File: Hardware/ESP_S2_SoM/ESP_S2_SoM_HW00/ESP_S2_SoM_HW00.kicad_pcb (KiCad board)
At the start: 6 copper layers, 29.5 x 24.7 mm, 55 parts, among them J1 DF40C-60DP-0.4V(51), J2 Bare PCB USB C, SW401 SW_Push, SW402 SW_Push, U201 BQ24075RGTR, U301 MIC5528-3.3YMT-T5, U401 ESP32-S2FH4, Y601 Crystal_GND24_Small

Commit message: ESP32 data is done
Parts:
- moved C407 21.5 mm to (136.7, 91.0), turned to 45 degrees
- moved L401 20.9 mm to (135.6, 90.4), turned to -45 degrees
- moved C406 19.9 mm to (134.5, 90.3), turned to -90 degrees
- moved ANT401 14.9 mm to (129.5, 90.3), turned to 180 degrees
- moved C401 3.19 mm to (127.8, 92.8), turned to 180 degrees
- moved C402 3.02 mm to (127.8, 96.0), turned to 0 degrees
- moved Y601 2.85 mm to (127.8, 94.4), turned to 90 degrees
- moved R406 2.21 mm to (133.9, 95.4)
- moved R405 2.21 mm to (134.5, 94.8)
- moved R407 2.21 mm to (135.0, 94.3)
- moved R408 2.21 mm to (133.4, 95.9)
- moved C410 1.17 mm to (138.0, 93.1)
- moved C403 1.17 mm to (129.9, 95.7)
- moved C404 1.17 mm to (132.6, 92.4)
- moved C408 1.17 mm to (135.1, 91.9)
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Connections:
- J1 pad 42: IO39 -> IO41 (x2)
- J1 pad 44: IO40 -> IO39 (x2)
- J1 pad 46: IO41 -> IO40 (x2)
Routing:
- net IO0: track 0.00 -> 16.7 mm, vias 0 -> 2
- net /100_Connectors/D+: track 14.9 -> 19.9 mm
- net Net-(C401-Pad1): track 1.98 -> 4.11 mm
- net Net-(U401-XTAL_N): track 5.15 -> 7.28 mm
- net IO18: track 5.65 -> 7.55 mm, vias 0 -> 1
- net IO8: track 9.76 -> 11.3 mm
- net SPI6: track 8.13 -> 6.59 mm
- net IO33: track 15.2 -> 16.6 mm
- net /100_Connectors/D-: track 16.2 -> 17.4 mm
- net IO41: track 19.5 -> 18.3 mm
- net SPI5: track 5.61 -> 4.60 mm
- net IO38: track 15.1 -> 16.1 mm
- net SPI4: track 5.68 -> 4.77 mm
- net IO5: track 11.7 -> 12.5 mm
- net IO14: track 7.39 -> 8.20 mm
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
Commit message: working on power routing
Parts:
- moved R101 1.60 mm to (128.6, 108.0)
- moved R102 1.60 mm to (128.6, 108.0)
- moved C404 0.83 mm to (132.6, 91.6), turned to 90 degrees
- moved C402 0.40 mm to (127.8, 95.6)
- moved Y601 0.40 mm to (127.8, 94.0)
- moved C401 0.40 mm to (127.8, 92.4)
- moved R403 0.33 mm to (133.9, 91.6), turned to -90 degrees
- moved C414 0.30 mm to (133.2, 91.6), turned to 90 degrees
- moved ANT401 0.22 mm to (129.6, 90.1)
- moved C403 0.17 mm to (130.0, 95.8)
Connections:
- J1 pad 10: unconnected-(J1-Pad10) -> VBUS (x2)
- J1 pad 12: unconnected-(J1-Pad12) -> VBUS (x2)
- J1 pad 14: unconnected-(J1-Pad14) -> /VSYS (x2)
- J1 pad 16: unconnected-(J1-Pad16) -> /VSYS (x2)
- J1 pad 18: unconnected-(J1-Pad18) -> +3V3 (x2)
- J1 pad 20: unconnected-(J1-Pad20) -> +3V3 (x2)
- J1 pad 22: unconnected-(J1-Pad22) -> GND (x2)
- J1 pad 24: unconnected-(J1-Pad24) -> GND (x2)
- J1 pad 4: unconnected-(J1-Pad4) -> /VBAT (x2)
- J1 pad 48: /100_Connectors/TX0 -> /100_Connectors/RX0 (x2)
- J1 pad 50: /100_Connectors/RX0 -> /100_Connectors/TX0 (x2)
- J1 pad 6: unconnected-(J1-Pad6) -> /VBAT (x2)
- J1 pad 8: unconnected-(J1-Pad8) -> /VBAT (x2)
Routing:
- net GND: track 1.91 -> 34.4 mm, vias 32 -> 65
- net VBUS: track 5.60 -> 37.5 mm, vias 0 -> 4
- net /VBAT: track 1.81 -> 22.7 mm
- net /400_ESP32/EN: track 1.89 -> 17.9 mm, vias 0 -> 2
- net IO15: track 6.40 -> 21.4 mm, vias 0 -> 2
- net +3V3: track 11.6 -> 25.7 mm, vias 0 -> 11
- net /100_Connectors/CC2: track 0.00 -> 4.38 mm, vias 0 -> 2
- net /100_Connectors/CC1: track 0.00 -> 3.57 mm
- net SPI6: track 6.59 -> 8.76 mm
- net /100_Connectors/D+: track 19.9 -> 18.2 mm, vias 2 -> 1
- net IO42: track 16.5 -> 15.3 mm
- net IO33: track 16.6 -> 15.8 mm
- net /100_Connectors/D-: track 17.4 -> 17.1 mm, vias 2 -> 1

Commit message: Routing is done
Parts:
- added C101: 100n, Capacitor_SMD:C_0201_0603Metric, B.Cu at (142.6, 99.9)
- added R103: 220k, Resistor_SMD:R_0201_0603Metric, B.Cu at (142.6, 101.2)
- added R104: 470k, Resistor_SMD:R_0201_0603Metric, B.Cu at (142.6, 100.5)
- ANT401, C406, C407, L401: moved to F.Cu
- moved R406 1.60 mm to (132.4, 94.9), turned to -45 degrees
- moved R405 1.35 mm to (133.4, 94.0), turned to -45 degrees
- moved R407 0.91 mm to (134.4, 95.0)
- moved C407 0.64 mm to (136.3, 91.5), turned to -135 degrees
- renumbered J1 to J101, J2 to J102
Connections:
- net Net-(ANT401-A) renamed /400_ESP32/ANT
- J101 pad 3: IO1 -> /100_Connectors/BATTERY_TEMP (x2)
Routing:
- net /VSYS: track 3.93 -> 35.1 mm, vias 0 -> 4
- net VBUS: track 37.5 -> 51.4 mm, vias 4 -> 5
- net /100_Connectors/BATTERY_TEMP: track 0.00 -> 12.0 mm, vias 0 -> 2
- net +3V3: track 25.7 -> 34.5 mm, vias 11 -> 13
- net /400_ESP32/ANT: track 0.00 -> 4.43 mm
- net /100_Connectors/D-: track 17.1 -> 21.5 mm, vias 1 -> 3
- net GND: track 34.4 -> 38.7 mm, vias 65 -> 68
- net /400_ESP32/LNA_IN: track 0.00 -> 3.75 mm, vias 0 -> 1
- net IO1: track 14.6 -> 10.9 mm
- net /VBAT: track 22.7 -> 24.9 mm, vias 2 -> 4
- net /100_Connectors/D+: track 18.2 -> 20.4 mm, vias 1 -> 2
- net /100_Connectors/CC2: track 4.38 -> 6.41 mm
- net SPI7: track 3.99 -> 4.86 mm
- added copper zone on F.Cu, net +3V3
- added copper zone on In2.Cu, net +3V3
- added copper zone on F.Cu, net /400_ESP32/ANT
- added copper zone on F.Cu, net /VSYS

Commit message: Routing done, ready for prod
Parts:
- added G***: LOGO, Component_lib:puma_logo_14mm, F.Cu at (132.8, 99.9)
- moved R404 1.30 mm to (135.7, 98.9)
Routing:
- net GND: track 38.7 -> 90.3 mm, vias 68 -> 83
- net /VSYS: track 35.1 -> 39.0 mm
- net VBUS: track 51.4 -> 49.7 mm
- net /VBAT: track 24.9 -> 26.2 mm
- net +3V3: track 34.5 -> 35.4 mm
- net IO15: track 21.4 -> 20.7 mm
- net IO18: track 7.88 -> 8.51 mm
- added copper zone on B.Cu, net GND
- added copper zone on F.Cu, net GND
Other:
- board text added: "CHG"
- board text added: "EN"
- board text added: "IO0"
- board text added: "IO15"
- board text added: "PG"
- board text added: "PSoM ESP32S2 HW00"

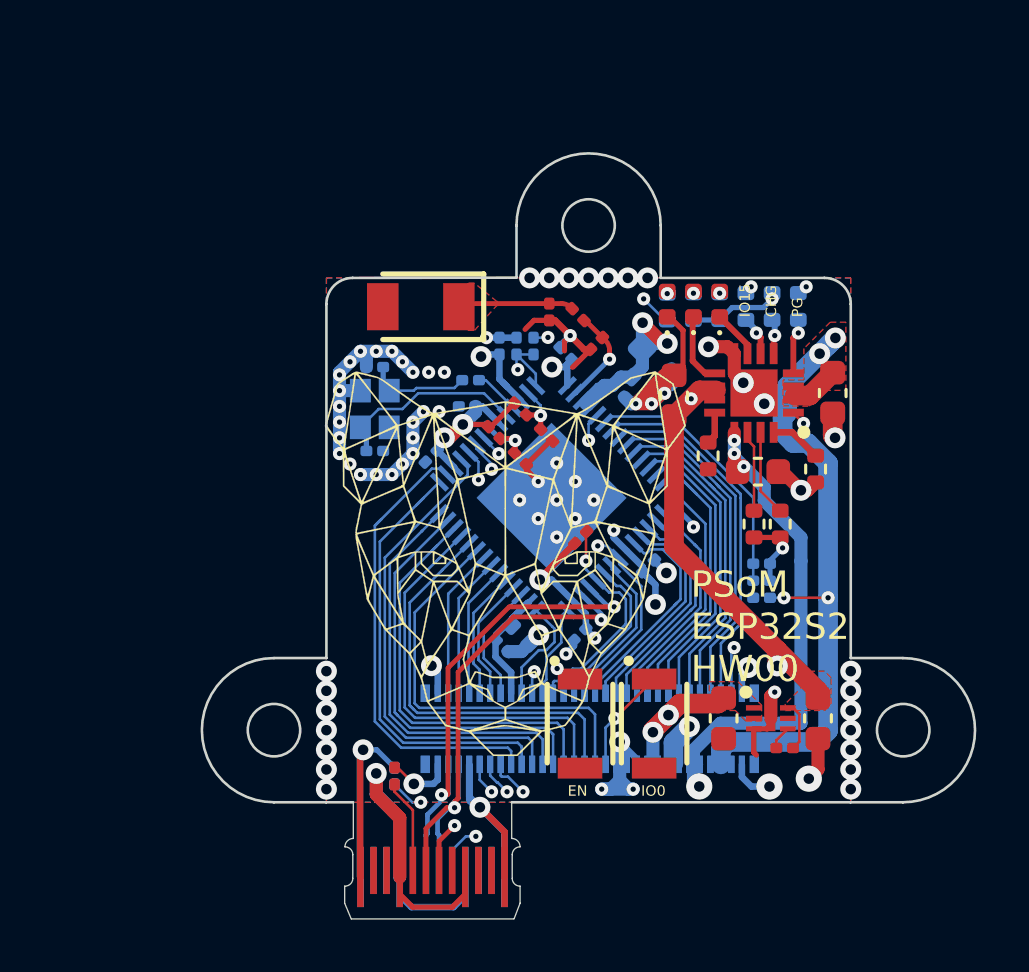
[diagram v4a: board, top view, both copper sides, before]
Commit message: quick pinout adjustement
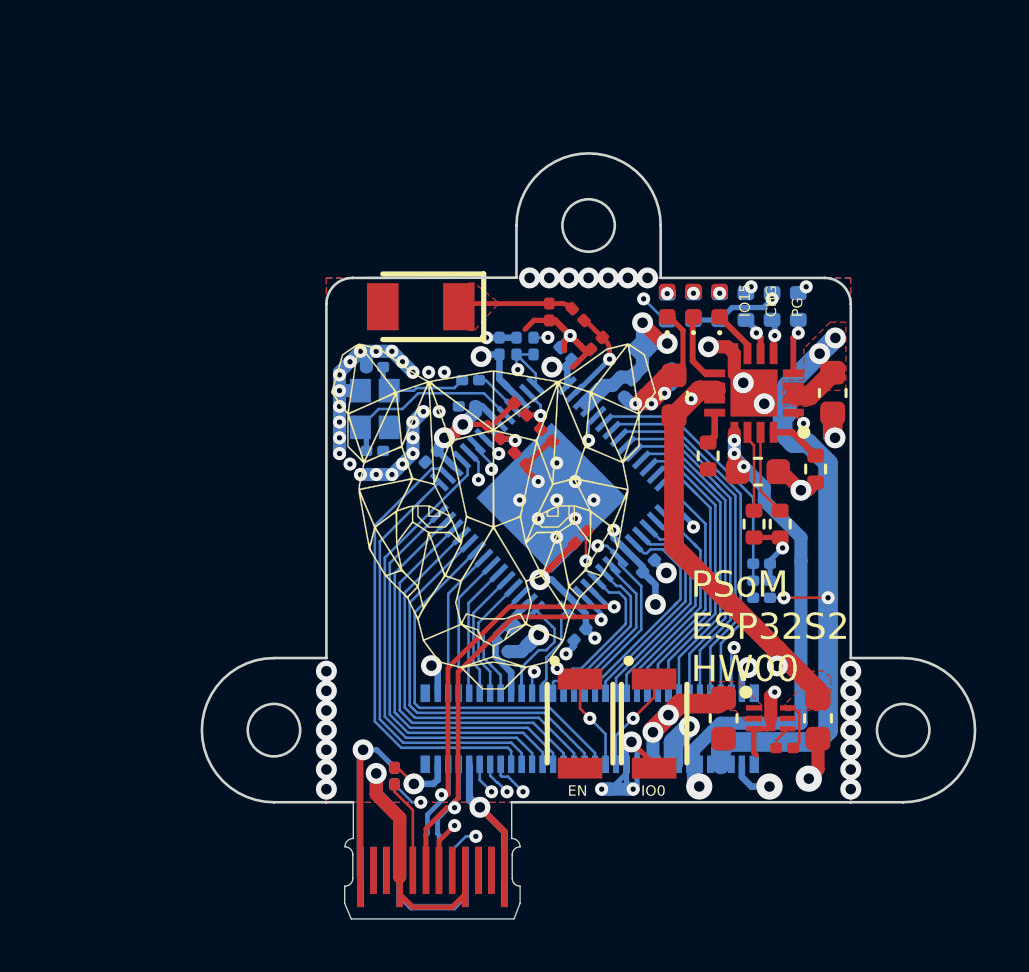
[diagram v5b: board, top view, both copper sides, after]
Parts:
- moved G*** 1.86 mm to (132.3, 98.1)
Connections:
- C414 pad 1: /400_ESP32/EN -> /100_Connectors/EN
- J101 pad 26: GND -> IO0 (x2)
- J101 pad 28: IO0 -> /100_Connectors/EN (x2)
- R403 pad 2: /400_ESP32/EN -> /100_Connectors/EN
- SW401 pad 1: /400_ESP32/EN -> /100_Connectors/EN
- U401 pad 56: /400_ESP32/EN -> /100_Connectors/EN
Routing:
- net /100_Connectors/EN: track 0.00 -> 21.9 mm, vias 0 -> 3
- net /400_ESP32/EN: track 18.2 -> 0.00 mm, vias 2 -> 0
- net IO33: track 15.8 -> 14.9 mm
- net IO34: track 16.0 -> 15.2 mm
- net IO35: track 15.9 -> 15.2 mm
- net IO36: track 16.0 -> 15.5 mm
